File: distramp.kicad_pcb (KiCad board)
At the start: 2 copper layers, 50 x 50 mm, 27 parts, among them P1 ANT, P2 OUT, P3 OUT, P4 OUT, P5 OUT, U1 MAAL-010704, U2 TPS796xxDCQ

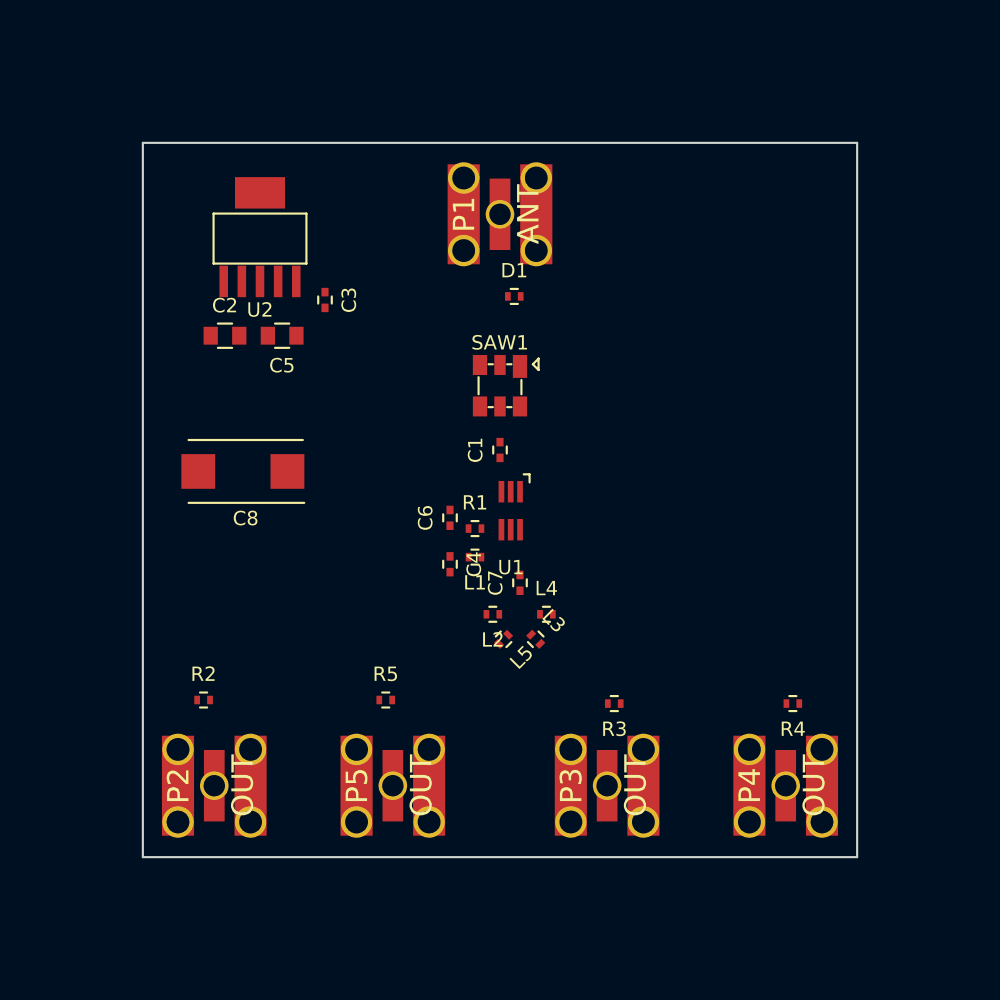
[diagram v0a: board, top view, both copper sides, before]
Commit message: RF routed
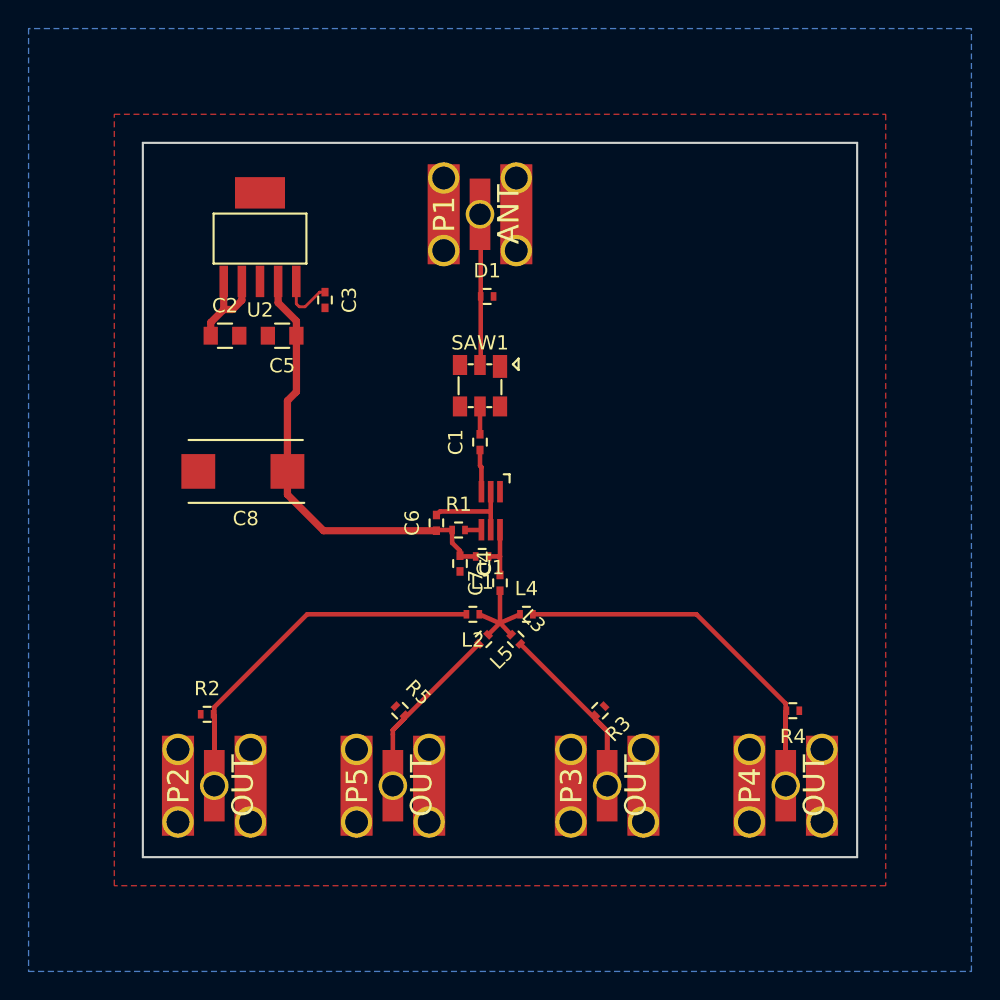
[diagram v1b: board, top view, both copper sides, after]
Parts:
- moved D1 1.90 mm to (84.1, 70.8)
- moved C1 1.50 mm to (83.6, 81.0)
- moved C7 1.40 mm to (85.0, 90.8)
- moved L2 1.40 mm to (83.1, 93.0)
- moved L3 1.40 mm to (86.1, 94.8)
- moved L4 1.40 mm to (86.8, 93.0)
- moved L5 1.40 mm to (83.8, 94.8)
- moved P1 1.40 mm to (83.6, 65.0)
- moved SAW1 1.40 mm to (83.6, 77.0)
- moved U1 1.40 mm to (84.3, 85.8)
- moved R5 1.25 mm to (78.0, 99.8), turned to 315 degrees
- moved R1 1.15 mm to (82.1, 87.1)
- moved R3 1.12 mm to (92.0, 99.8), turned to 225 degrees
- moved R2 1.03 mm to (64.5, 100.0)
- moved C6 1.01 mm to (80.5, 86.6)
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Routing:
- net Vcc_3V: track 0.00 -> 31.5 mm
- net Net-(L4-Pad2): track 0.00 -> 31.4 mm
- net Net-(L2-Pad2): track 0.00 -> 30.9 mm
- net Net-(L3-Pad2): track 0.00 -> 17.8 mm
- net Net-(L5-Pad2): track 0.00 -> 13.8 mm
- net Net-(D1-Pad1): track 0.00 -> 10.6 mm
- net Net-(C7-Pad1): track 0.00 -> 7.68 mm
- net +5V: track 0.00 -> 7.03 mm
- net GND: track 0.00 -> 6.57 mm
- net Net-(C3-Pad1): track 0.00 -> 4.09 mm
- net Net-(C7-Pad2): track 0.00 -> 3.97 mm
- net Net-(C1-Pad1): track 0.00 -> 2.96 mm
- net Net-(C1-Pad2): track 0.00 -> 1.95 mm
- net Net-(R1-Pad2): track 0.00 -> 1.16 mm
- added copper zone on B.Cu, net GND
- added copper zone on F.Cu, net GND
- added copper zone on In1.Cu, net GND
- added copper zone on In2.Cu, net GND
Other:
- copper layers 2 -> 4
- net class Default: clearance 0.2 -> 0.15; trace_width 0.25 -> 0.15; via_drill 0.4 -> 0.3
- rule trace_clearance: 0.2 -> 0.15
- rule trace_min: 0.2 -> 0.15
- rule via_min_size: 0.4 -> 0.6

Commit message: More PCB work
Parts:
- moved C8 4.24 mm to (70.0, 86.0)
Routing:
- net GND: track 6.57 -> 307.2 mm, vias 0 -> 92
- net Vcc_3V: track 31.5 -> 30.0 mm
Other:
- board text added: "434MHz Distribution Amp"

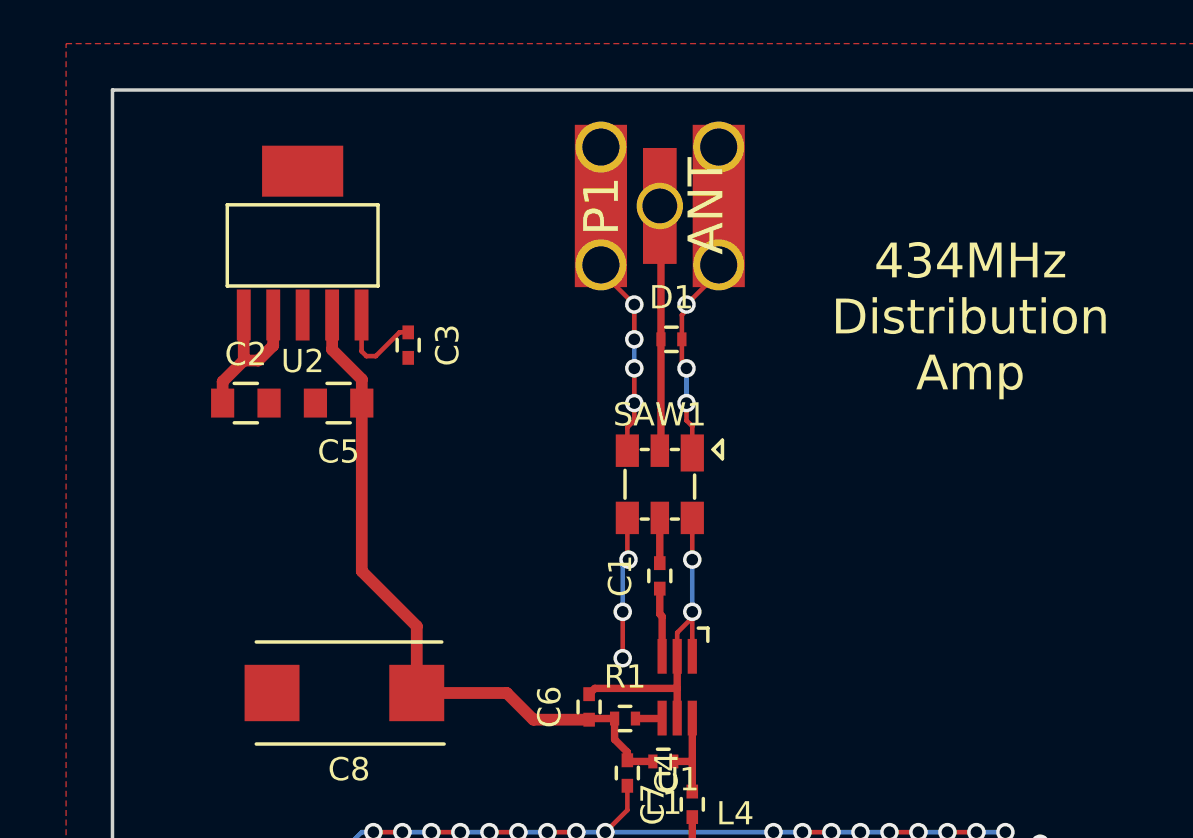
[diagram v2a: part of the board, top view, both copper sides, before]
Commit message: Add Power Connector
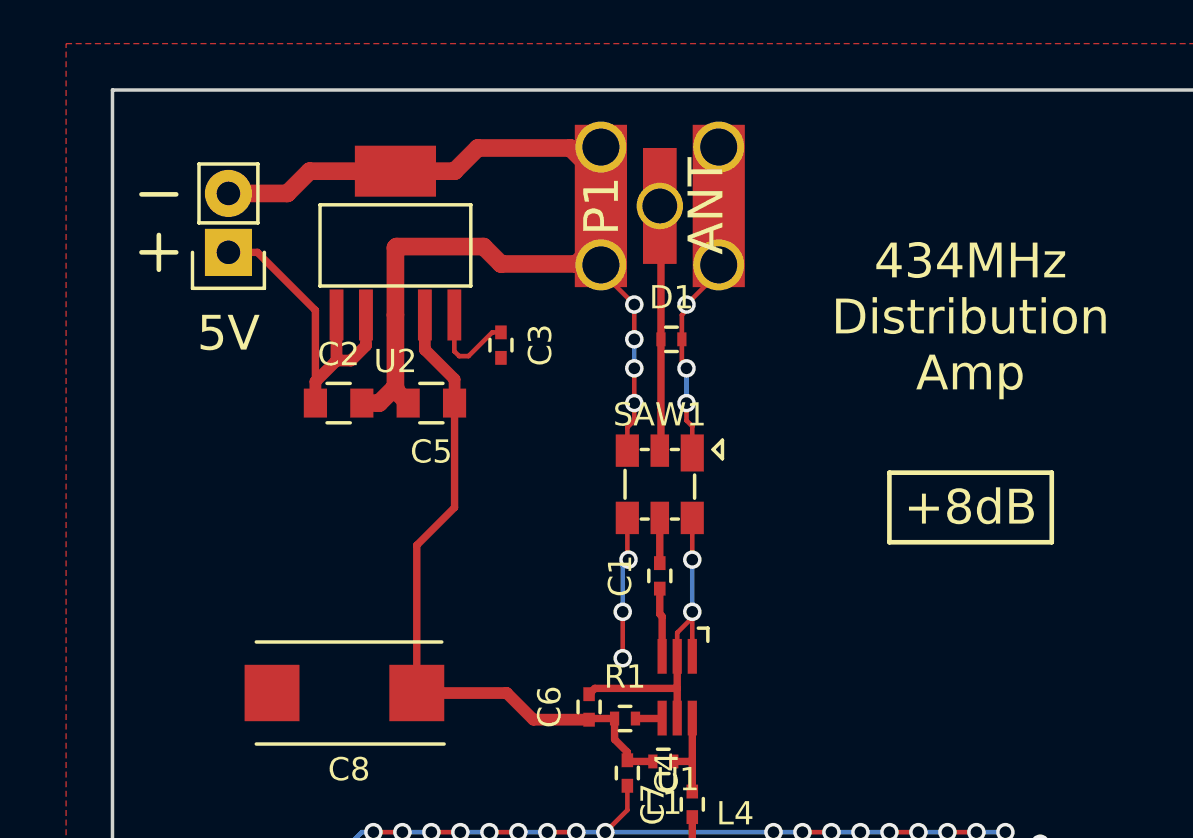
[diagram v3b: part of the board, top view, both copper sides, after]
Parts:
- added P6: PWR, Pin_Headers:Pin_Header_Straight_1x02, F.Cu at (65.0, 67.0)
- moved C2 4.00 mm to (69.8, 73.5)
- moved C3 4.00 mm to (76.8, 71.0)
- moved C5 4.00 mm to (73.8, 73.5)
- moved U2 4.00 mm to (72.2, 69.7)
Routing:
- net GND: track 307.2 -> 345.5 mm
- net +5V: track 7.03 -> 14.9 mm
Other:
- board text added: "+8dB"
- board text added: "5V"
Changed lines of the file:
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@@
 (kicad_pcb (version 4) (host pcbnew 4.0.2-stable)
   (general
-    (links 82)
+    (links 84)
     (no_connects 0)
     (area 59.924999 59.924999 110.075001 110.075001)
     (thickness 1.6)
-    (drawings 5)
-    (tracks 331)
+    (drawings 14)
+    (tracks 354)
     (zones 0)
-    (modules 27)
+    (modules 28)
     (nets 15)
   )
@@
   )
   (setup
-    (last_trace_width 0.508)
+    (last_trace_width 0.32)
     (user_trace_width 0.18)
     (user_trace_width 0.2)
@@
   )
   (module Capacitors_SMD:C_0805 (layer F.Cu)
-    (at 65.75 73.5)
+    (at 69.75 73.5)
     (descr "Capacitor SMD 0805, reflow soldering, AVX (see smccp.pdf)")
     (tags "capacitor 0805")
@@
   )
   (module Capacitors_SMD:C_0402 (layer F.Cu)
-    (at 72.75 71 270)
+    (at 76.75 71 270)
     (descr "Capacitor SMD 0402, reflow soldering, AVX (see smccp.pdf)")
     (tags "capacitor 0402")
@@
   )
   (module Capacitors_SMD:C_0805 (layer F.Cu)
-    (at 69.75 73.5 180)
+    (at 73.75 73.5 180)
     (descr "Capacitor SMD 0805, reflow soldering, AVX (see smccp.pdf)")
     (tags "capacitor 0805")
@@
   )
   (module "Custom Parts:SOT-223-6" (layer F.Cu)
-    (at 68.2 69.7)
+    (at 72.2 69.7)
     (fp_text reference U2 (at 0 2) (layer F.SilkS)
       (effects (font (size 1 1) (thickness 0.15)))
@@
       (net 4 GND))
   )
+  (module Pin_Headers:Pin_Header_Straight_1x02 (layer F.Cu)
+    (at 65 67 180)
+    (descr "Through hole pin header")
+    (tags "pin header")
+    (fp_text reference P6 (at 0 -5.1 180) (layer F.SilkS) hide
+      (effects (font (size 1 1) (thickness 0.15)))
+    )
+    (fp_text value PWR (at 0 -3.1 180) (layer F.Fab) hide
+      (effects (font (size 1 1) (thickness 0.15)))
+    )
+    (fp_line (start 1.27 1.27) (end 1.27 3.81) (layer F.SilkS) (width 0.15))
+    (fp_line (start 1.55 -1.55) (end 1.55 0) (layer F.SilkS) (width 0.15))
+    (fp_line (start -1.75 -1.75) (end -1.75 4.3) (layer F.CrtYd) (width 0.05))
+    (fp_line (start 1.75 -1.75) (end 1.75 4.3) (layer F.CrtYd) (width 0.05))
+    (fp_line (start -1.75 -1.75) (end 1.75 -1.75) (layer F.CrtYd) (width 0.05))
+    (fp_line (start -1.75 4.3) (end 1.75 4.3) (layer F.CrtYd) (width 0.05))
+    (fp_line (start 1.27 1.27) (end -1.27 1.27) (layer F.SilkS) (width 0.15))
+    (fp_line (start -1.55 0) (end -1.55 -1.55) (layer F.SilkS) (width 0.15))
+    (fp_line (start -1.55 -1.55) (end 1.55 -1.55) (layer F.SilkS) (width 0.15))
+    (fp_line (start -1.27 1.27) (end -1.27 3.81) (layer F.SilkS) (width 0.15))
+    (fp_line (start -1.27 3.81) (end 1.27 3.81) (layer F.SilkS) (width 0.15))
+    (pad 1 thru_hole rect (at 0 0 180) (size 2.032 2.032) (drill 1.016) (layers *.Cu *.Mask F.SilkS)
+      (net 3 +5V))
+    (pad 2 thru_hole oval (at 0 2.54 180) (size 2.032 2.032) (drill 1.016) (layers *.Cu *.Mask F.SilkS)
+      (net 4 GND))
+    (model Pin_Headers.3dshapes/Pin_Header_Straight_1x02.wrl
+      (at (xyz 0 -0.05 0))
+      (scale (xyz 1 1 1))
+      (rotate (xyz 0 0 90))
+    )
+  )
+  (gr_text 5V (at 65 70.5) (layer F.SilkS)
+    (effects (font (size 1.5 1.5) (thickness 0.3)))
+  )
+  (gr_line (start 93.5 76.5) (end 93.5 79.5) (angle 90) (layer F.SilkS) (width 0.2))
+  (gr_line (start 100.5 76.5) (end 93.5 76.5) (angle 90) (layer F.SilkS) (width 0.2))
+  (gr_line (start 100.5 79.5) (end 100.5 76.5) (angle 90) (layer F.SilkS) (width 0.2))
+  (gr_line (start 93.5 79.5) (end 100.5 79.5) (angle 90) (layer F.SilkS) (width 0.2))
+  (gr_text +8dB (at 97 78) (layer F.SilkS)
+    (effects (font (size 1.5 1.5) (thickness 0.3)))
+  )
+  (gr_line (start 61.25 64.5) (end 62.75 64.5) (angle 90) (layer F.SilkS) (width 0.2))
+  (gr_line (start 62 66.25) (end 62 67.75) (angle 90) (layer F.SilkS) (width 0.2))
+  (gr_line (start 61.25 67) (end 62.75 67) (angle 90) (layer F.SilkS) (width 0.2))
   (gr_text "434MHz\nDistribution\nAmp" (at 97 69.8) (layer F.SilkS)
     (effects (font (size 1.5 1.5) (thickness 0.3)))
@@
   (segment (start 83.6 82.6) (end 83.69976 82.69976) (width 0.32) (layer F.Cu) (net 1))
   (segment (start 83.6 80.4) (end 83.6 78.45) (width 0.32) (layer F.Cu) (net 2))
-  (segment (start 66.93 69.7) (end 66.93 71.02) (width 0.508) (layer F.Cu) (net 3))
-  (segment (start 66.285 71.665) (end 65.66 71.665) (width 0.508) (layer F.Cu) (net 3))
-  (segment (start 66.93 71.02) (end 66.285 71.665) (width 0.508) (layer F.Cu) (net 3))
-  (segment (start 65.66 69.7) (end 65.66 71.665) (width 0.508) (layer F.Cu) (net 3))
-  (segment (start 64.75 72.575) (end 64.75 73.5) (width 0.508) (layer F.Cu) (net 3))
-  (segment (start 65.66 71.665) (end 64.75 72.575) (width 0.508) (layer F.Cu) (net 3))
+  (segment (start 68.75 72.575) (end 68.75 69.5) (width 0.32) (layer F.Cu) (net 3))
+  (segment (start 66.25 67) (end 65 67) (width 0.32) (layer F.Cu) (net 3) (status 800000))
+  (segment (start 68.75 69.5) (end 66.25 67) (width 0.32) (layer F.Cu) (net 3))
+  (segment (start 70.93 69.7) (end 70.93 71.02) (width 0.508) (layer F.Cu) (net 3))
+  (segment (start 70.285 71.665) (end 69.66 71.665) (width 0.508) (layer F.Cu) (net 3))
+  (segment (start 70.93 71.02) (end 70.285 71.665) (width 0.508) (layer F.Cu) (net 3))
+  (segment (start 69.66 69.7) (end 69.66 71.665) (width 0.508) (layer F.Cu) (net 3))
+  (segment (start 68.75 72.575) (end 68.75 73.5) (width 0.508) (layer F.Cu) (net 3))
+  (segment (start 69.66 71.665) (end 68.75 72.575) (width 0.508) (layer F.Cu) (net 3))
+  (segment (start 70.75 73.5) (end 71.5 73.5) (width 0.762) (layer F.Cu) (net 4) (status 400000))
+  (segment (start 71.5 73.5) (end 72.2 72.8) (width 0.762) (layer F.Cu) (net 4))
+  (segment (start 72.2 69.7) (end 72.2 72.8) (width 0.762) (layer F.Cu) (net 4) (status 400000))
+  (segment (start 72.2 72.8) (end 72.2 72.95) (width 0.762) (layer F.Cu) (net 4))
+  (segment (start 72.2 72.95) (end 72.75 73.5) (width 0.762) (layer F.Cu) (net 4) (status 800000))
+  (segment (start 81.06 65) (end 81.06 66.44) (width 0.762) (layer F.Cu) (net 4) (status C00000))
+  (segment (start 81.06 66.44) (end 80 67.5) (width 0.762) (layer F.Cu) (net 4) (status C00000))
+  (segment (start 80 67.5) (end 76.75 67.5) (width 0.762) (layer F.Cu) (net 4) (status 400000))
+  (segment (start 76.75 67.5) (end 76 66.75) (width 0.762) (layer F.Cu) (net 4))
+  (segment (start 76 66.75) (end 72.25 66.75) (width 0.762) (layer F.Cu) (net 4))
+  (segment (start 72.25 66.75) (end 72.2 66.8) (width 0.762) (layer F.Cu) (net 4))
+  (segment (start 72.2 66.8) (end 72.2 69.7) (width 0.762) (layer F.Cu) (net 4) (status 800000))
+  (segment (start 81.06 65) (end 81.06 63.81) (width 0.762) (layer F.Cu) (net 4) (status C00000))
+  (segment (start 81.06 63.81) (end 79.75 62.5) (width 0.762) (layer F.Cu) (net 4) (status 400000))
+  (segment (start 74.75 63.5) (end 72.2 63.5) (width 0.762) (layer F.Cu) (net 4) (status 800000))
+  (segment (start 75.75 62.5) (end 74.75 63.5) (width 0.762) (layer F.Cu) (net 4))
+  (segment (start 79.75 62.5) (end 75.75 62.5) (width 0.762) (layer F.Cu) (net 4))
+  (segment (start 65 64.46) (end 67.54 64.46) (width 0.762) (layer F.Cu) (net 4) (status 400000))
+  (segment (start 68.5 63.5) (end 72.2 63.5) (width 0.762) (layer F.Cu) (net 4) (status 800000))
+  (segment (start 67.54 64.46) (end 68.5 63.5) (width 0.762) (layer F.Cu) (net 4))
   (segment (start 61 106) (end 61 101.2) (width 0.508) (layer F.Cu) (net 4))
   (segment (start 61.2 109.2) (end 61 109) (width 0.508) (layer F.Cu) (net 4))
@@
   (segment (start 84.35 87.08096) (end 84.35 85.8) (width 0.32) (layer F.Cu) (net 4))
   (segment (start 84.35 85.8) (end 84.35 84.41904) (width 0.32) (layer F.Cu) (net 4))
-  (segment (start 70.74 69.7) (end 70.74 71.265) (width 0.2) (layer F.Cu) (net 5))
-  (segment (start 72.375 70.45) (end 72.75 70.45) (width 0.2) (layer F.Cu) (net 5))
-  (segment (start 71.35 71.475) (end 72.375 70.45) (width 0.2) (layer F.Cu) (net 5))
-  (segment (start 70.95 71.475) (end 71.35 71.475) (width 0.2) (layer F.Cu) (net 5))
-  (segment (start 70.74 71.265) (end 70.95 71.475) (width 0.2) (layer F.Cu) (net 5))
-  (segment (start 73.12 86) (end 73.12 83.12) (width 0.508) (layer F.Cu) (net 6))
-  (segment (start 70.75 80.75) (end 70.75 73.5) (width 0.508) (layer F.Cu) (net 6))
-  (segment (start 73.12 83.12) (end 70.75 80.75) (width 0.508) (layer F.Cu) (net 6))
+  (segment (start 74.74 69.7) (end 74.74 71.265) (width 0.2) (layer F.Cu) (net 5))
+  (segment (start 76.375 70.45) (end 76.75 70.45) (width 0.2) (layer F.Cu) (net 5))
+  (segment (start 75.35 71.475) (end 76.375 70.45) (width 0.2) (layer F.Cu) (net 5))
+  (segment (start 74.95 71.475) (end 75.35 71.475) (width 0.2) (layer F.Cu) (net 5))
+  (segment (start 74.74 71.265) (end 74.95 71.475) (width 0.2) (layer F.Cu) (net 5))
+  (segment (start 74.75 73.5) (end 74.75 78) (width 0.32) (layer F.Cu) (net 6) (status 400000))
+  (segment (start 73.12 79.63) (end 73.12 86) (width 0.32) (layer F.Cu) (net 6) (status 800000))
+  (segment (start 74.75 78) (end 73.12 79.63) (width 0.32) (layer F.Cu) (net 6))
   (segment (start 80.55 87.15) (end 78.15 87.15) (width 0.508) (layer F.Cu) (net 6))
+  (segment (start 78.15 87.15) (end 77 86) (width 0.508) (layer F.Cu) (net 6))
   (segment (start 77 86) (end 73.12 86) (width 0.508) (layer F.Cu) (net 6))
-  (segment (start 78.15 87.15) (end 77 86) (width 0.508) (layer F.Cu) (net 6))
-  (segment (start 69.47 69.7) (end 69.47 71.195) (width 0.508) (layer F.Cu) (net 6))
-  (segment (start 69.47 71.195) (end 70.75 72.475) (width 0.508) (layer F.Cu) (net 6))
-  (segment (start 70.75 72.475) (end 70.75 73.5) (width 0.508) (layer F.Cu) (net 6))
+  (segment (start 73.47 69.7) (end 73.47 71.195) (width 0.508) (layer F.Cu) (net 6))
+  (segment (start 73.47 71.195) (end 74.75 72.475) (width 0.508) (layer F.Cu) (net 6))
+  (segment (start 74.75 72.475) (end 74.75 73.5) (width 0.508) (layer F.Cu) (net 6))
   (segment (start 82.2 88.9) (end 82.2 88.55) (width 0.32) (layer F.Cu) (net 6))
   (segment (start 81.65 88) (end 81.65 87.1) (width 0.32) (layer F.Cu) (net 6))
